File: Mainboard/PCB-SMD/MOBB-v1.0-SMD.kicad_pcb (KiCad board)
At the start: 2 copper layers, 85.6 x 49.7 mm, 68 parts, among them P1 AUX 1-3, P14 EXTRA Pins, P2 VUSB, P3 +3.3V, P4 Pit Limiter, P5 Rotary Encoders, P6 BTN 1-32, P7 LED, Q1 NPN, Q2 NPN, Q3 NPN, Q4 NPN, U1 74HC4051, U2 74HC4051, U3 74HC4051, U4 74HC4051, U5 Teensy3.2

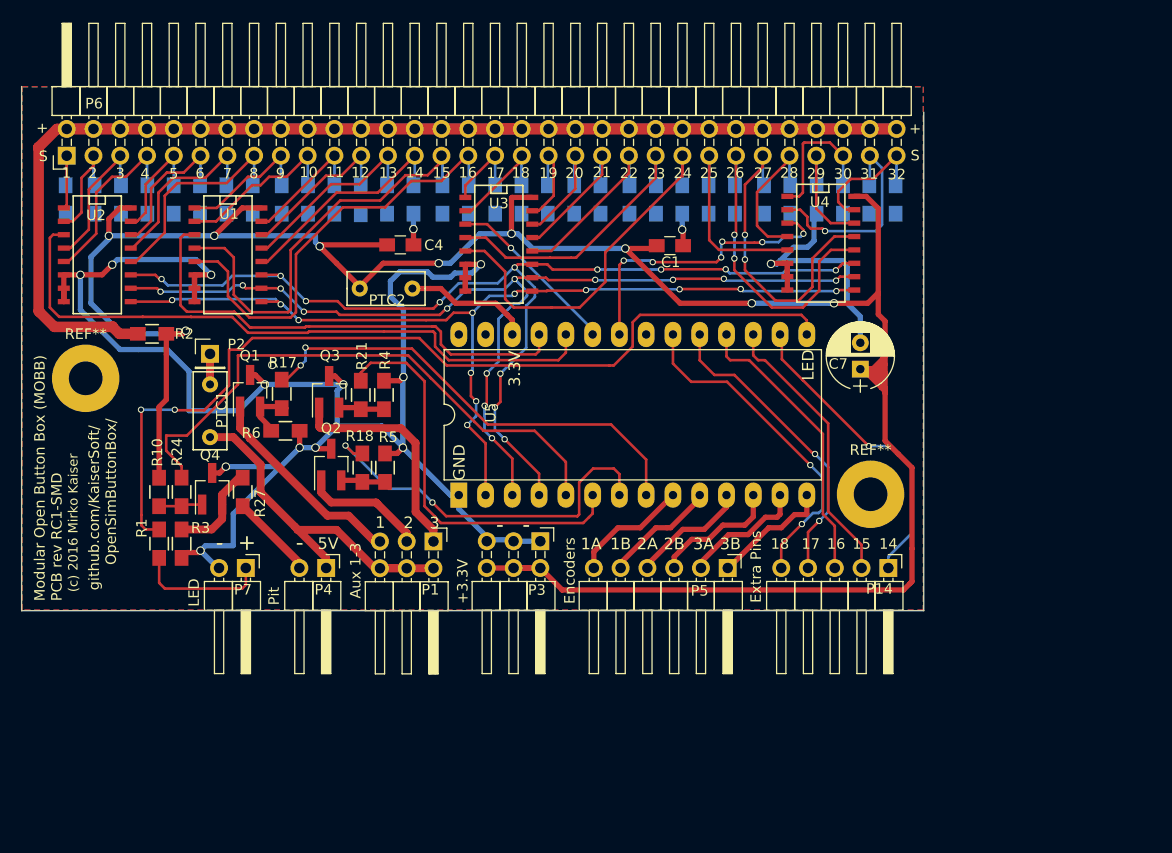
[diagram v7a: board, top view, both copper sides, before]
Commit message: * added ground vias
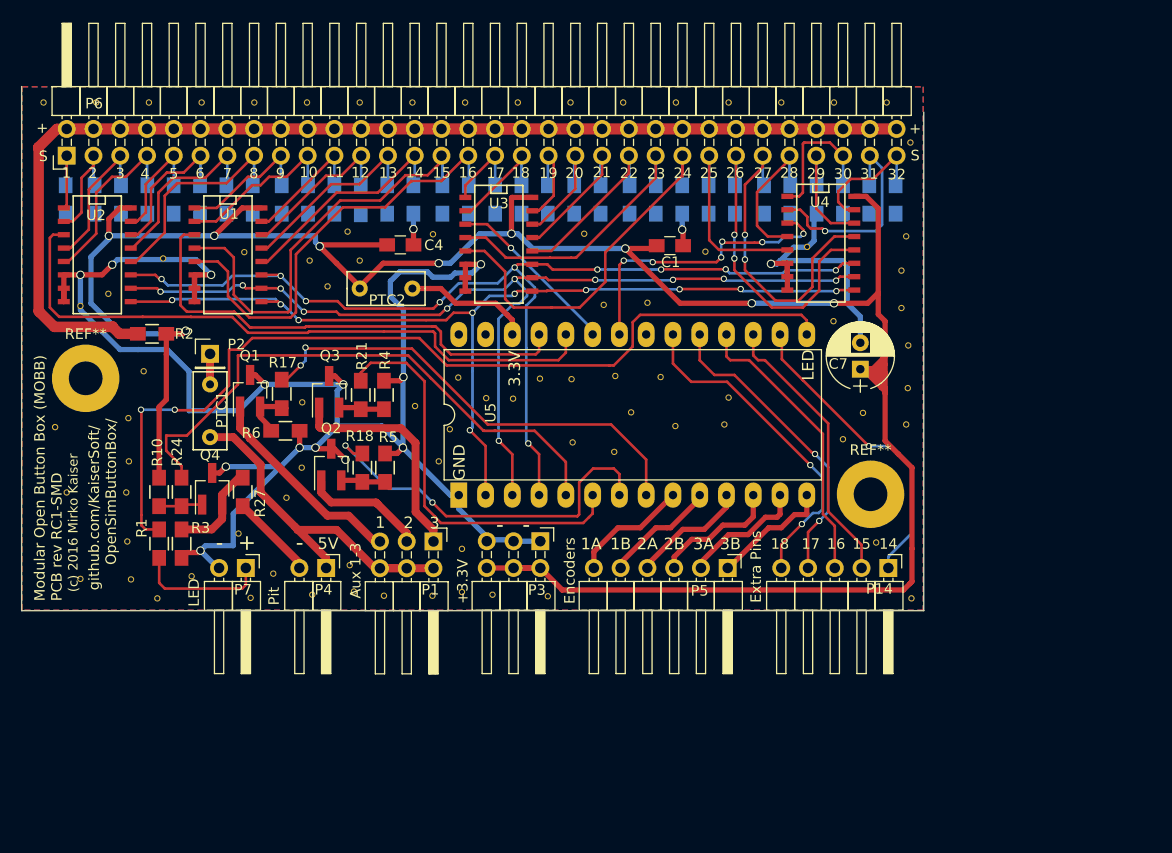
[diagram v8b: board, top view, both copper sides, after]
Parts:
- added Ref**: Val**, MOBB-KiCad-Lib:VIA-W0.6mm-H0.4mm, F.Cu at (259.4, 119.6)
- added Ref**: Val**, MOBB-KiCad-Lib:VIA-W0.6mm-H0.4mm, F.Cu at (214.3, 109.0)
- added Ref**: Val**, MOBB-KiCad-Lib:VIA-W0.6mm-H0.4mm, F.Cu at (180.9, 115.8)
- added Ref**: Val**, MOBB-KiCad-Lib:VIA-W0.6mm-H0.4mm, F.Cu at (216.8, 122.7)
- added Ref**: Val**, MOBB-KiCad-Lib:VIA-W0.6mm-H0.4mm, F.Cu at (240.2, 110.7)
- added Ref**: Val**, MOBB-KiCad-Lib:VIA-W0.6mm-H0.4mm, F.Cu at (234.7, 115.5)
- added Ref**: Val**, MOBB-KiCad-Lib:VIA-W0.6mm-H0.4mm, F.Cu at (230.6, 115.8)
- added Ref**: Val**, MOBB-KiCad-Lib:VIA-W0.6mm-H0.4mm, F.Cu at (228.7, 109.0)
- added Ref**: Val**, MOBB-KiCad-Lib:VIA-W0.6mm-H0.4mm, F.Cu at (188.8, 111.3)
- added Ref**: Val**, MOBB-KiCad-Lib:VIA-W0.6mm-H0.4mm, F.Cu at (196.4, 110.8)
- added Ref**: Val**, MOBB-KiCad-Lib:VIA-W0.6mm-H0.4mm, F.Cu at (183.6, 114.7)
- added Ref**: Val**, MOBB-KiCad-Lib:VIA-W0.6mm-H0.4mm, F.Cu at (259.4, 123.7)
- added Ref**: Val**, MOBB-KiCad-Lib:VIA-W0.6mm-H0.4mm, F.Cu at (178.5, 127.3)
- added Ref**: Val**, MOBB-KiCad-Lib:VIA-W0.6mm-H0.4mm, F.Cu at (179.6, 133.6)
- added Ref**: Val**, MOBB-KiCad-Lib:VIA-W0.6mm-H0.4mm, F.Cu at (180.9, 141.8)
- added Ref**: Val**, MOBB-KiCad-Lib:VIA-W0.6mm-H0.4mm, F.Cu at (185.4, 126.5)
- added Ref**: Val**, MOBB-KiCad-Lib:VIA-W0.6mm-H0.4mm, F.Cu at (186.9, 122.0)
- added Ref**: Val**, MOBB-KiCad-Lib:VIA-W0.6mm-H0.4mm, F.Cu at (207.4, 111.5)
- added Ref**: Val**, MOBB-KiCad-Lib:VIA-W0.6mm-H0.4mm, F.Cu at (202.7, 111.5)
- added Ref**: Val**, MOBB-KiCad-Lib:VIA-W0.6mm-H0.4mm, F.Cu at (204.3, 114.0)
- added Ref**: Val**, MOBB-KiCad-Lib:VIA-W0.6mm-H0.4mm, F.Cu at (221.9, 124.7)
- added Ref**: Val**, MOBB-KiCad-Lib:VIA-W0.6mm-H0.4mm, F.Cu at (219.4, 124.6)
- added Ref**: Val**, MOBB-KiCad-Lib:VIA-W0.6mm-H0.4mm, F.Cu at (195.9, 137.4)
- added Ref**: Val**, MOBB-KiCad-Lib:VIA-W0.6mm-H0.4mm, F.Cu at (214.9, 130.6)
- added Ref**: Val**, MOBB-KiCad-Lib:VIA-W0.6mm-H0.4mm, F.Cu at (215.9, 127.5)
- added Ref**: Val**, MOBB-KiCad-Lib:VIA-W0.6mm-H0.4mm, F.Cu at (212.7, 125.3)
- added Ref**: Val**, MOBB-KiCad-Lib:VIA-W0.6mm-H0.4mm, F.Cu at (201.9, 125.0)
- added Ref**: Val**, MOBB-KiCad-Lib:VIA-W0.6mm-H0.4mm, F.Cu at (201.9, 131.2)
- added Ref**: Val**, MOBB-KiCad-Lib:VIA-W0.6mm-H0.4mm, F.Cu at (200.4, 134.1)
- added Ref**: Val**, MOBB-KiCad-Lib:VIA-W0.6mm-H0.4mm, F.Cu at (191.4, 141.5)
- added Ref**: Val**, MOBB-KiCad-Lib:VIA-W0.6mm-H0.4mm, F.Cu at (185.7, 141.8)
- added Ref**: Val**, MOBB-KiCad-Lib:VIA-W0.6mm-H0.4mm, F.Cu at (197.1, 143.6)
- added Ref**: Val**, MOBB-KiCad-Lib:VIA-W0.6mm-H0.4mm, F.Cu at (199.2, 141.2)
- added Ref**: Val**, MOBB-KiCad-Lib:VIA-W0.6mm-H0.4mm, F.Cu at (185.5, 130.6)
- added Ref**: Val**, MOBB-KiCad-Lib:VIA-W0.6mm-H0.4mm, F.Cu at (188.2, 143.6)
- added Ref**: Val**, MOBB-KiCad-Lib:VIA-W0.6mm-H0.4mm, F.Cu at (202.9, 143.2)
- added Ref**: Val**, MOBB-KiCad-Lib:VIA-W0.6mm-H0.4mm, F.Cu at (206.4, 140.4)
- added Ref**: Val**, MOBB-KiCad-Lib:VIA-W0.6mm-H0.4mm, F.Cu at (206.8, 142.9)
- added Ref**: Val**, MOBB-KiCad-Lib:VIA-W0.6mm-H0.4mm, F.Cu at (209.7, 143.3)
- added Ref**: Val**, MOBB-KiCad-Lib:VIA-W0.6mm-H0.4mm, F.Cu at (214.3, 143.3)
- added Ref**: Val**, MOBB-KiCad-Lib:VIA-W0.6mm-H0.4mm, F.Cu at (217.1, 138.9)
- added Ref**: Val**, MOBB-KiCad-Lib:VIA-W0.6mm-H0.4mm, F.Cu at (217.1, 143.0)
- added Ref**: Val**, MOBB-KiCad-Lib:VIA-W0.6mm-H0.4mm, F.Cu at (220.0, 143.2)
- added Ref**: Val**, MOBB-KiCad-Lib:VIA-W0.6mm-H0.4mm, F.Cu at (225.2, 143.4)
- added Ref**: Val**, MOBB-KiCad-Lib:VIA-W0.6mm-H0.4mm, F.Cu at (185.2, 133.6)
- added Ref**: Val**, MOBB-KiCad-Lib:VIA-W0.6mm-H0.4mm, F.Cu at (259.8, 143.6)
- added Ref**: Val**, MOBB-KiCad-Lib:VIA-W0.6mm-H0.4mm, F.Cu at (256.4, 138.3)
- added Ref**: Val**, MOBB-KiCad-Lib:VIA-W0.6mm-H0.4mm, F.Cu at (259.2, 127.1)
- added Ref**: Val**, MOBB-KiCad-Lib:VIA-W0.6mm-H0.4mm, F.Cu at (258.8, 116.0)
- added Ref**: Val**, MOBB-KiCad-Lib:VIA-W0.6mm-H0.4mm, F.Cu at (258.8, 112.5)
- added Ref**: Val**, MOBB-KiCad-Lib:VIA-W0.6mm-H0.4mm, F.Cu at (259.2, 109.2)
- added Ref**: Val**, MOBB-KiCad-Lib:VIA-W0.6mm-H0.4mm, F.Cu at (252.3, 117.3)
- added Ref**: Val**, MOBB-KiCad-Lib:VIA-W0.6mm-H0.4mm, F.Cu at (253.2, 128.5)
- added Ref**: Val**, MOBB-KiCad-Lib:VIA-W0.6mm-H0.4mm, F.Cu at (255.2, 126.0)
- added Ref**: Val**, MOBB-KiCad-Lib:VIA-W0.6mm-H0.4mm, F.Cu at (242.4, 124.5)
- added Ref**: Val**, MOBB-KiCad-Lib:VIA-W0.6mm-H0.4mm, F.Cu at (185.3, 138.2)
- added Ref**: Val**, MOBB-KiCad-Lib:VIA-W0.6mm-H0.4mm, F.Cu at (242.0, 127.1)
- added Ref**: Val**, MOBB-KiCad-Lib:VIA-W0.6mm-H0.4mm, F.Cu at (237.3, 127.2)
- added Ref**: Val**, MOBB-KiCad-Lib:VIA-W0.6mm-H0.4mm, F.Cu at (233.2, 126.0)
- added Ref**: Val**, MOBB-KiCad-Lib:VIA-W0.6mm-H0.4mm, F.Cu at (231.6, 129.7)
- added Ref**: Val**, MOBB-KiCad-Lib:VIA-W0.6mm-H0.4mm, F.Cu at (227.6, 128.8)
- added Ref**: Val**, MOBB-KiCad-Lib:VIA-W0.6mm-H0.4mm, F.Cu at (235.9, 122.6)
- added Ref**: Val**, MOBB-KiCad-Lib:VIA-W0.6mm-H0.4mm, F.Cu at (231.7, 122.5)
- added Ref**: Val**, MOBB-KiCad-Lib:VIA-W0.6mm-H0.4mm, F.Cu at (227.5, 122.8)
- added Ref**: Val**, MOBB-KiCad-Lib:VIA-W0.6mm-H0.4mm, F.Cu at (224.5, 122.8)
- added Ref**: Val**, MOBB-KiCad-Lib:VIA-W0.6mm-H0.4mm, F.Cu at (257.4, 96.5)
- added Ref**: Val**, MOBB-KiCad-Lib:VIA-W0.6mm-H0.4mm, F.Cu at (249.8, 110.2)
- added Ref**: Val**, MOBB-KiCad-Lib:VIA-W0.6mm-H0.4mm, F.Cu at (252.4, 96.5)
- added Ref**: Val**, MOBB-KiCad-Lib:VIA-W0.6mm-H0.4mm, F.Cu at (247.4, 96.5)
- added Ref**: Val**, MOBB-KiCad-Lib:VIA-W0.6mm-H0.4mm, F.Cu at (242.4, 96.5)
- added Ref**: Val**, MOBB-KiCad-Lib:VIA-W0.6mm-H0.4mm, F.Cu at (237.4, 96.5)
- added Ref**: Val**, MOBB-KiCad-Lib:VIA-W0.6mm-H0.4mm, F.Cu at (232.4, 96.5)
- added Ref**: Val**, MOBB-KiCad-Lib:VIA-W0.6mm-H0.4mm, F.Cu at (227.4, 96.5)
- added Ref**: Val**, MOBB-KiCad-Lib:VIA-W0.6mm-H0.4mm, F.Cu at (222.4, 96.5)
- added Ref**: Val**, MOBB-KiCad-Lib:VIA-W0.6mm-H0.4mm, F.Cu at (217.4, 96.5)
- added Ref**: Val**, MOBB-KiCad-Lib:VIA-W0.6mm-H0.4mm, F.Cu at (212.4, 96.5)
- added Ref**: Val**, MOBB-KiCad-Lib:VIA-W0.6mm-H0.4mm, F.Cu at (207.4, 96.5)
- added Ref**: Val**, MOBB-KiCad-Lib:VIA-W0.6mm-H0.4mm, F.Cu at (259.6, 100.3)
- added Ref**: Val**, MOBB-KiCad-Lib:VIA-W0.6mm-H0.4mm, F.Cu at (202.4, 96.5)
- added Ref**: Val**, MOBB-KiCad-Lib:VIA-W0.6mm-H0.4mm, F.Cu at (197.4, 96.5)
- added Ref**: Val**, MOBB-KiCad-Lib:VIA-W0.6mm-H0.4mm, F.Cu at (192.4, 96.5)
- added Ref**: Val**, MOBB-KiCad-Lib:VIA-W0.6mm-H0.4mm, F.Cu at (187.4, 96.5)
- added Ref**: Val**, MOBB-KiCad-Lib:VIA-W0.6mm-H0.4mm, F.Cu at (182.4, 96.5)
- added Ref**: Val**, MOBB-KiCad-Lib:VIA-W0.6mm-H0.4mm, F.Cu at (177.4, 96.5)
- added Ref**: Val**, MOBB-KiCad-Lib:VIA-W0.6mm-H0.4mm, F.Cu at (206.2, 108.8)
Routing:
- net Net-(U1-Pad11): track 100.9 -> 98.4 mm, vias 12 -> 10
- net GND: track 195.6 -> 197.9 mm, vias 15 -> 16
- net Net-(U1-Pad10): track 96.1 -> 95.0 mm, vias 13 -> 11
- net Net-(U1-Pad9): track 91.7 -> 91.1 mm, vias 12 -> 10
- net (no net): vias 1 -> 0
